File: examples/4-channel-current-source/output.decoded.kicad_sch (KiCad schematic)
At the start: 25 parts, among them IC12 ULQ2003AQDRQ1, Q4 BSS84Q-13-F, Q5 BSS84Q-13-F, Q6 BSS84Q-13-F, Q7 BSS84Q-13-F

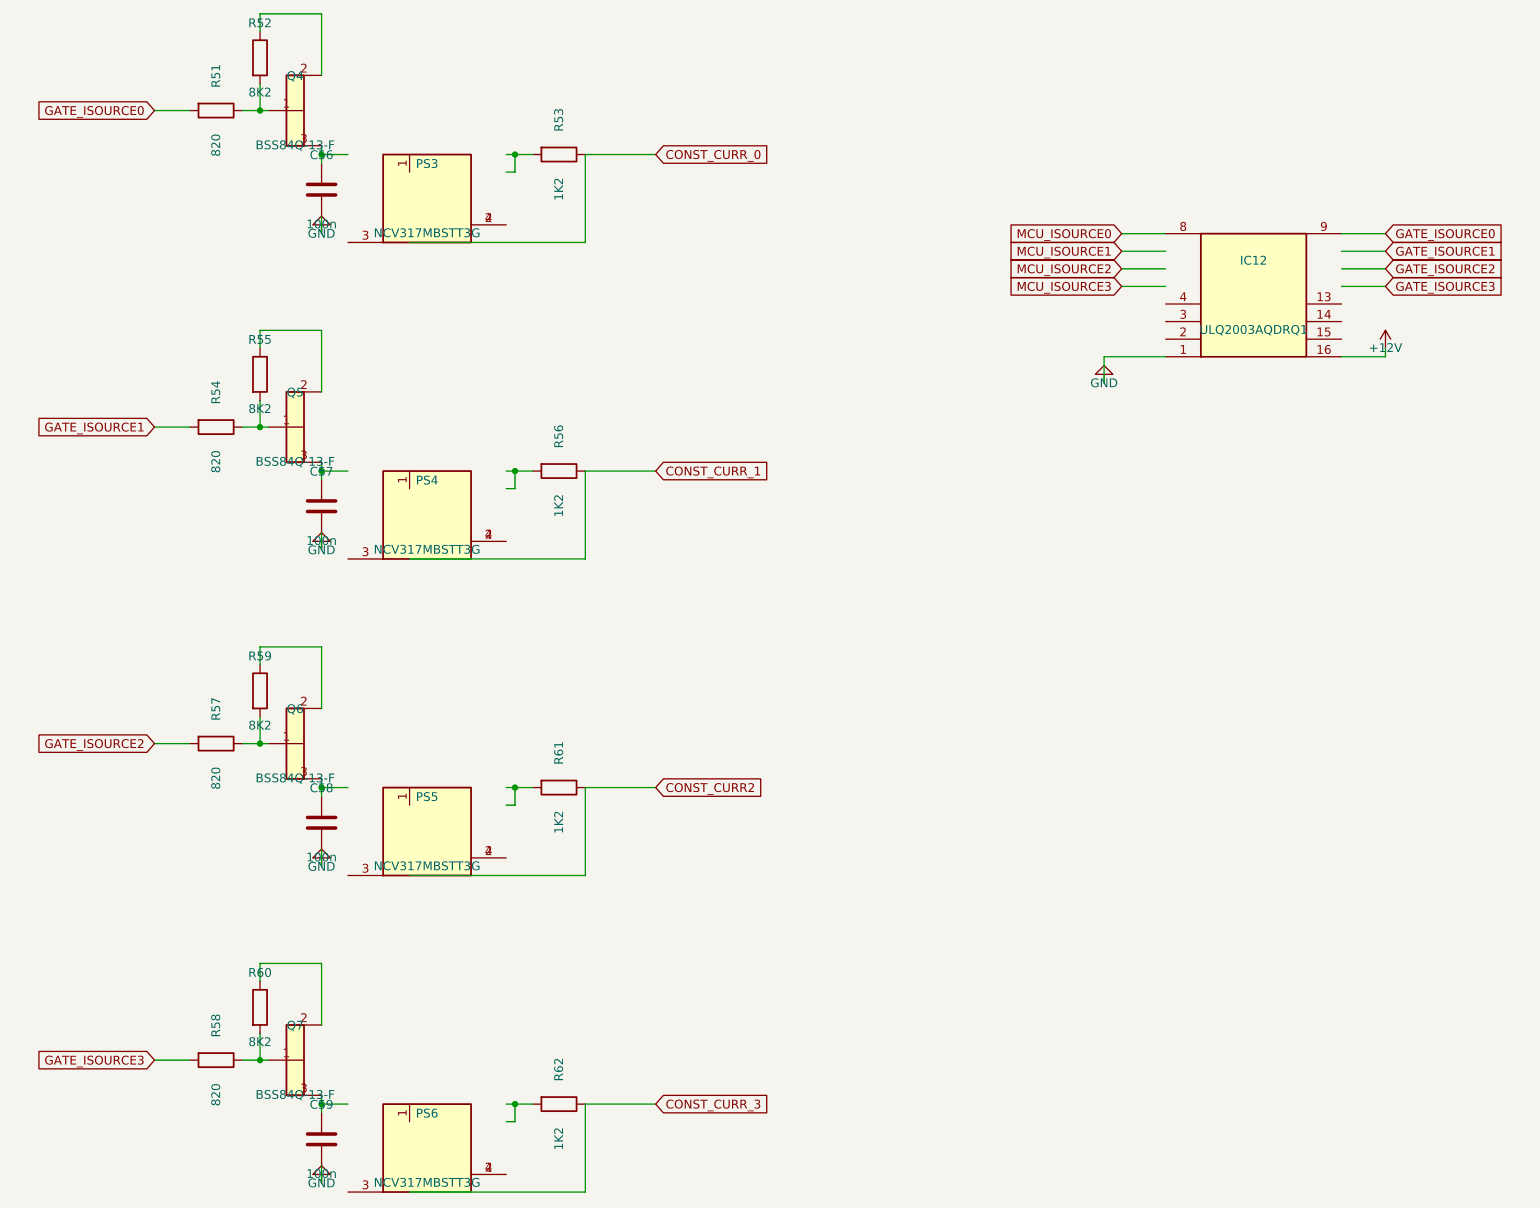
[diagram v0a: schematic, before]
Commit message: Add footprint lookup table for TOKN decoder
- Add footprints.json with comprehensive lookup table:
  - Common passive sizes (0402, 0603, 0805, etc.)
  - IC packages (SOIC, TSSOP, QFN, LQFP, etc.)
  - Specific parts (MCP2551, MAX232, ATmega, STM32, etc.)
  - Transistors, regulators, op-amps, and more

- Update tokn_decoder.py to auto-populate footprints:
  - Priority: explicit > package hint > part match > passive type
  - Handles size codes (0603) for passives automatically

Decoded schematics now have proper footprints ready for PCB layout.
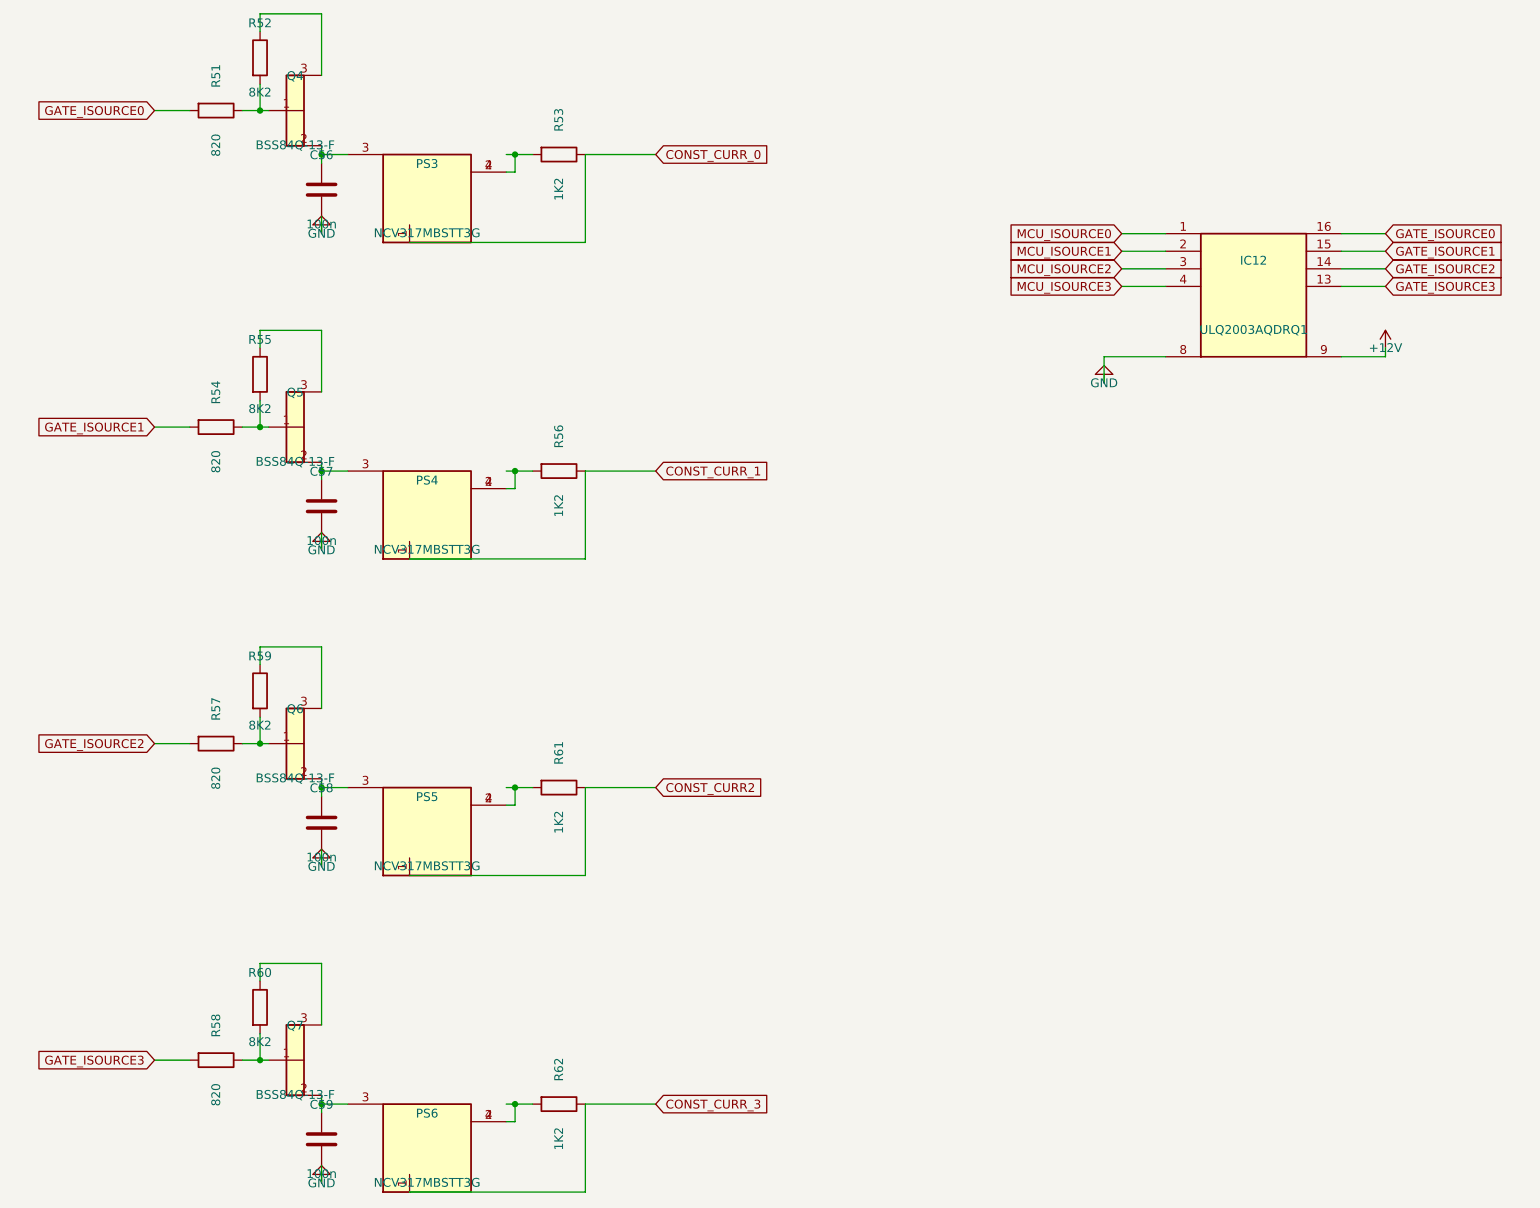
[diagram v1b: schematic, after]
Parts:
- C56, C57, C58, C59: footprint (none) -> Capacitor_SMD:C_0603_1608Metric
- IC12: footprint SOIC-127 -> Package_SO:SOIC-16_3.9x9.9mm_P1.27mm
- PS3, PS4, PS5, PS6: footprint SOT230P700X175-4N -> (none)
- Q4, Q5, Q6, Q7: footprint SOT-23 -> Package_TO_SOT_SMD:SOT-23
- R51, R52, R53, R54, R55, R56, R57, R58, R59, R60, R61, R62: footprint 0603 -> Resistor_SMD:R_0603_1608Metric
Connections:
- net +12V: now also IC12.9; no longer IC12.16
- net CONST_CURR2: now also PS5.1
- net CONST_CURR_0: now also PS3.1
- net CONST_CURR_1: now also PS4.1
- net CONST_CURR_3: now also PS6.1
- net GATE_ISOURCE0: now also IC12.16; no longer IC12.9
- net GATE_ISOURCE1: now also IC12.15
- net GATE_ISOURCE2: now also IC12.14
- net GATE_ISOURCE3: now also IC12.13
- net GND: now also IC12.8; no longer IC12.1
- net MCU_ISOURCE0: now also IC12.1; no longer IC12.8
- net MCU_ISOURCE1: now also IC12.2
- net MCU_ISOURCE2: now also IC12.3
- net MCU_ISOURCE3: now also IC12.4
- net at R60.1: now also Q7.3; no longer Q7.2
- net at PS5.2, PS5.4: now also R61.2
- net at PS5.3: now also C58.1, Q6.2
- net at R55.1: now also Q5.3; no longer Q5.2
- net at C56.1: now also PS3.3, Q4.2; no longer Q4.3
- net at R59.1: now also Q6.3; no longer Q6.2
- net at R56.2: now also PS4.2, PS4.4
- net at PS4.3: now also C57.1, Q5.2
- net at R53.2: now also PS3.2, PS3.4
- net at R52.1: now also Q4.3; no longer Q4.2
- net at C59.1: now also PS6.3, Q7.2; no longer Q7.3
- net at PS6.2, PS6.4: now also R62.2
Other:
- moved on the sheet: PS3, PS4, PS5, PS6
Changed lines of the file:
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@@
       (at 74.93 51.99 0)
       (effects (font (size 1.27 1.27))))
-    (property "Footprint" ""
+    (property "Footprint" "Capacitor_SMD:C_0603_1608Metric"
       (at 74.93 46.99 0)
       (effects (font (size 1.27 1.27)) (hide yes)))
@@
       (at 74.93 97.71 0)
       (effects (font (size 1.27 1.27))))
-    (property "Footprint" ""
+    (property "Footprint" "Capacitor_SMD:C_0603_1608Metric"
       (at 74.93 92.71 0)
       (effects (font (size 1.27 1.27)) (hide yes)))
@@
       (at 74.93 143.43 0)
       (effects (font (size 1.27 1.27))))
-    (property "Footprint" ""
+    (property "Footprint" "Capacitor_SMD:C_0603_1608Metric"
       (at 74.93 138.43 0)
       (effects (font (size 1.27 1.27)) (hide yes)))
@@
       (at 74.93 189.15 0)
       (effects (font (size 1.27 1.27))))
-    (property "Footprint" ""
+    (property "Footprint" "Capacitor_SMD:C_0603_1608Metric"
       (at 74.93 184.15 0)
       (effects (font (size 1.27 1.27)) (hide yes)))
@@
       (at 209.55 67.22999999999999 0)
       (effects (font (size 1.27 1.27))))
-    (property "Footprint" "SOIC-127"
+    (property "Footprint" "Package_SO:SOIC-16_3.9x9.9mm_P1.27mm"
       (at 209.55 62.23 0)
       (effects (font (size 1.27 1.27)) (hide yes)))
@@
       (at 90.17 53.26 0)
       (effects (font (size 1.27 1.27))))
-    (property "Footprint" "SOT230P700X175-4N"
+    (property "Footprint" ""
       (at 90.17 48.26 0)
       (effects (font (size 1.27 1.27)) (hide yes)))
@@
       (at 90.17 98.98 0)
       (effects (font (size 1.27 1.27))))
-    (property "Footprint" "SOT230P700X175-4N"
+    (property "Footprint" ""
       (at 90.17 93.98 0)
       (effects (font (size 1.27 1.27)) (hide yes)))
@@
       (at 90.17 144.7 0)
       (effects (font (size 1.27 1.27))))
-    (property "Footprint" "SOT230P700X175-4N"
+    (property "Footprint" ""
       (at 90.17 139.7 0)
       (effects (font (size 1.27 1.27)) (hide yes)))
@@
       (at 90.17 190.42 0)
       (effects (font (size 1.27 1.27))))
-    (property "Footprint" "SOT230P700X175-4N"
+    (property "Footprint" ""
       (at 90.17 185.42 0)
       (effects (font (size 1.27 1.27)) (hide yes)))
@@
       (at 71.12 40.56 0)
       (effects (font (size 1.27 1.27))))
-    (property "Footprint" "SOT-23"
+    (property "Footprint" "Package_TO_SOT_SMD:SOT-23"
       (at 71.12 35.56 0)
       (effects (font (size 1.27 1.27)) (hide yes)))
@@
       (at 71.12 86.28 0)
       (effects (font (size 1.27 1.27))))
-    (property "Footprint" "SOT-23"
+    (property "Footprint" "Package_TO_SOT_SMD:SOT-23"
       (at 71.12 81.28 0)
       (effects (font (size 1.27 1.27)) (hide yes)))
@@
       (at 71.12 132.0 0)
       (effects (font (size 1.27 1.27))))
-    (property "Footprint" "SOT-23"
+    (property "Footprint" "Package_TO_SOT_SMD:SOT-23"
       (at 71.12 127.0 0)
       (effects (font (size 1.27 1.27)) (hide yes)))
@@
       (at 71.12 177.72 0)
       (effects (font (size 1.27 1.27))))
-    (property "Footprint" "SOT-23"
+    (property "Footprint" "Package_TO_SOT_SMD:SOT-23"
       (at 71.12 172.72 0)
       (effects (font (size 1.27 1.27)) (hide yes)))
@@
       (at 59.69 40.56 0)
       (effects (font (size 1.27 1.27))))
-    (property "Footprint" "0603"
+    (property "Footprint" "Resistor_SMD:R_0603_1608Metric"
       (at 59.69 35.56 0)
       (effects (font (size 1.27 1.27)) (hide yes)))
@@
       (at 66.04 32.94 0)
       (effects (font (size 1.27 1.27))))
-    (property "Footprint" "0603"
+    (property "Footprint" "Resistor_SMD:R_0603_1608Metric"
       (at 66.04 27.94 0)
       (effects (font (size 1.27 1.27)) (hide yes)))
@@
       (at 109.22 46.91 0)
       (effects (font (size 1.27 1.27))))
-    (property "Footprint" "0603"
+    (property "Footprint" "Resistor_SMD:R_0603_1608Metric"
       (at 109.22 41.91 0)
       (effects (font (size 1.27 1.27)) (hide yes)))
@@
       (at 59.69 86.28 0)
       (effects (font (size 1.27 1.27))))
-    (property "Footprint" "0603"
+    (property "Footprint" "Resistor_SMD:R_0603_1608Metric"
       (at 59.69 81.28 0)
       (effects (font (size 1.27 1.27)) (hide yes)))
@@
       (at 66.04 78.66 0)
       (effects (font (size 1.27 1.27))))
-    (property "Footprint" "0603"
+    (property "Footprint" "Resistor_SMD:R_0603_1608Metric"
       (at 66.04 73.66 0)
       (effects (font (size 1.27 1.27)) (hide yes)))
@@
       (at 109.22 92.63 0)
       (effects (font (size 1.27 1.27))))
-    (property "Footprint" "0603"
+    (property "Footprint" "Resistor_SMD:R_0603_1608Metric"
       (at 109.22 87.63 0)
       (effects (font (size 1.27 1.27)) (hide yes)))
@@
       (at 59.69 132.0 0)
       (effects (font (size 1.27 1.27))))
-    (property "Footprint" "0603"
+    (property "Footprint" "Resistor_SMD:R_0603_1608Metric"
       (at 59.69 127.0 0)
       (effects (font (size 1.27 1.27)) (hide yes)))
@@
       (at 59.69 177.72 0)
       (effects (font (size 1.27 1.27))))
-    (property "Footprint" "0603"
+    (property "Footprint" "Resistor_SMD:R_0603_1608Metric"
       (at 59.69 172.72 0)
       (effects (font (size 1.27 1.27)) (hide yes)))
@@
       (at 66.04 124.38 0)
       (effects (font (size 1.27 1.27))))
-    (property "Footprint" "0603"
+    (property "Footprint" "Resistor_SMD:R_0603_1608Metric"
       (at 66.04 119.38 0)
       (effects (font (size 1.27 1.27)) (hide yes)))
@@
       (at 66.04 170.1 0)
       (effects (font (size 1.27 1.27))))
-    (property "Footprint" "0603"
+    (property "Footprint" "Resistor_SMD:R_0603_1608Metric"
       (at 66.04 165.1 0)
       (effects (font (size 1.27 1.27)) (hide yes)))
@@
       (at 109.22 138.35 0)
       (effects (font (size 1.27 1.27))))
-    (property "Footprint" "0603"
+    (property "Footprint" "Resistor_SMD:R_0603_1608Metric"
       (at 109.22 133.35 0)
       (effects (font (size 1.27 1.27)) (hide yes)))
@@
       (at 109.22 184.07 0)
       (effects (font (size 1.27 1.27))))
-    (property "Footprint" "0603"
+    (property "Footprint" "Resistor_SMD:R_0603_1608Metric"
       (at 109.22 179.07 0)
       (effects (font (size 1.27 1.27)) (hide yes)))

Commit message: Fix decoder pin placement using TOKN pins section
- Use pin definitions from TOKN pins{REF}[N]: section instead of
  deriving positions from wire endpoints
- Calculate pin positions using standard dual-inline IC layout:
  pins 1-N/2 on left (top to bottom), N/2+1 to N on right (bottom to top)
- Include pin names from TOKN in generated lib_symbols
- Fix issue where pins with same net were merged to same position
- Regenerate all decoded schematics with correct pin placement
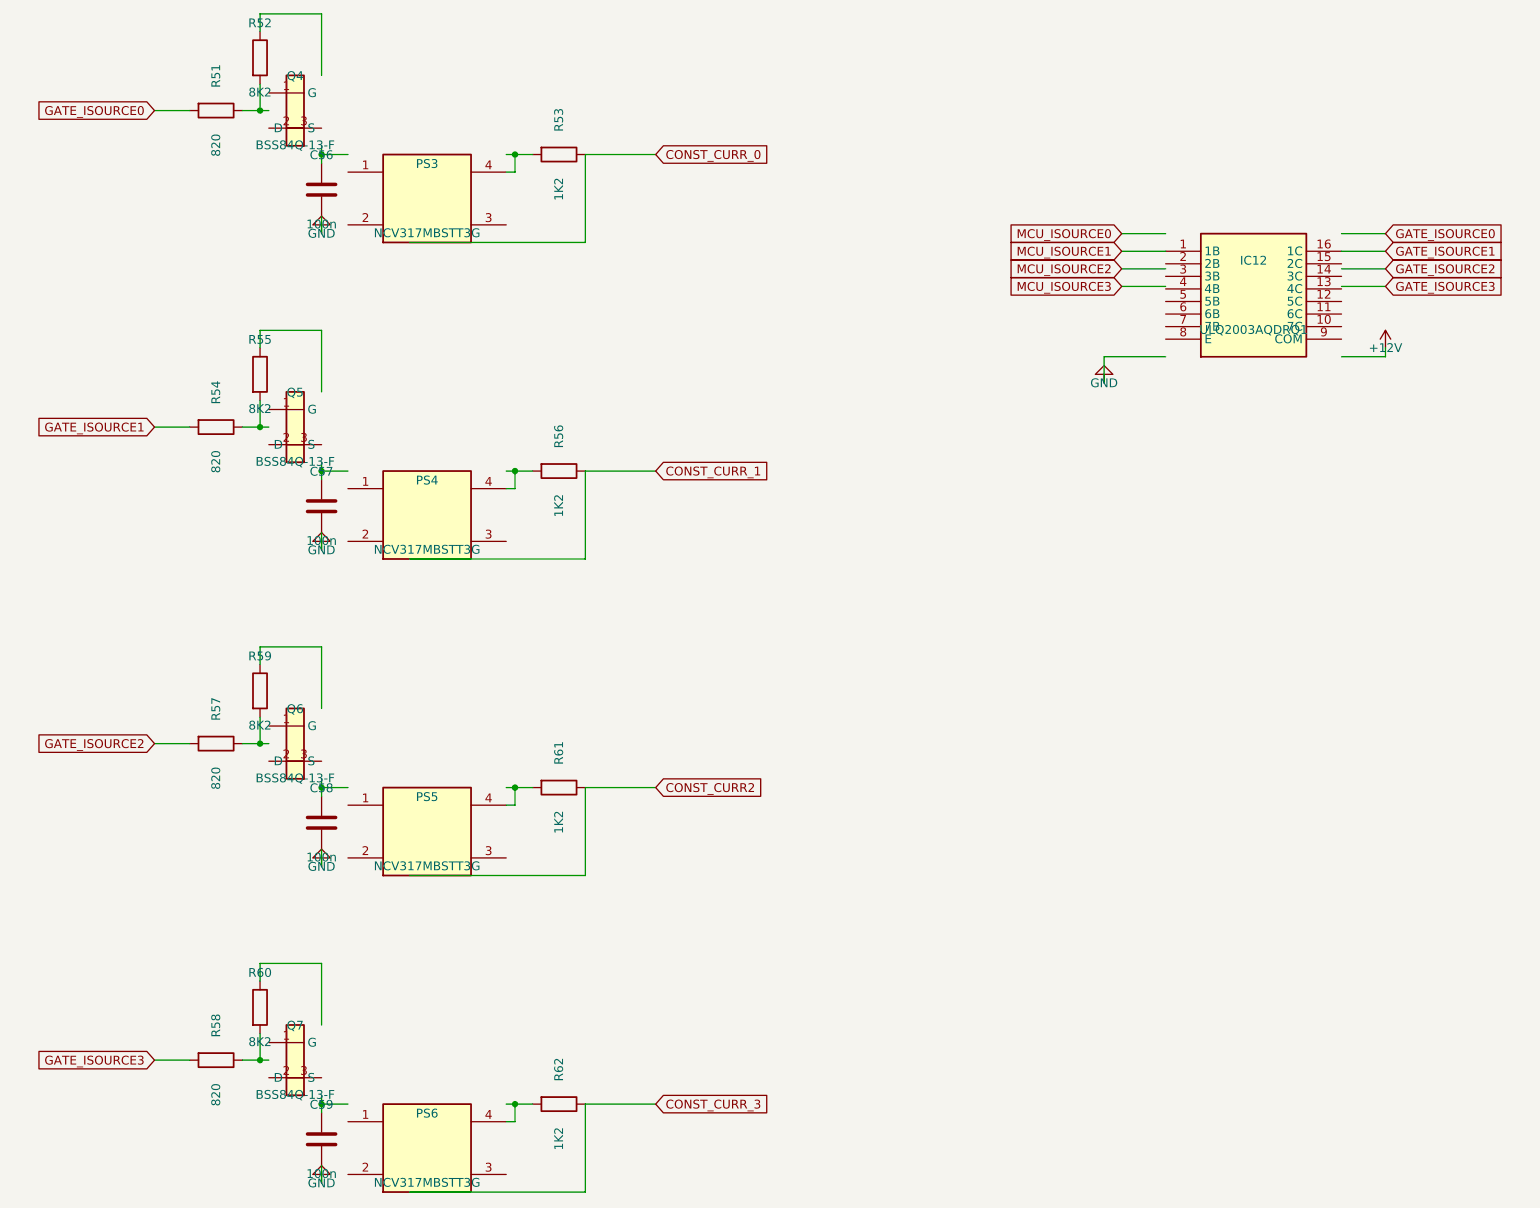
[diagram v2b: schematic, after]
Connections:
- net +12V: no longer IC12.9
- net CONST_CURR2: no longer PS5.1
- net CONST_CURR_0: no longer PS3.1
- net CONST_CURR_1: no longer PS4.1
- net CONST_CURR_3: no longer PS6.1
- net GATE_ISOURCE0: no longer IC12.16
- net GATE_ISOURCE1: now also IC12.16 (1C); no longer IC12.15
- net GATE_ISOURCE2: no longer IC12.14
- net GATE_ISOURCE3: no longer IC12.13
- net GND: no longer IC12.8
- net MCU_ISOURCE0: no longer IC12.1
- net MCU_ISOURCE1: now also IC12.1 (1B); no longer IC12.2
- net MCU_ISOURCE2: no longer IC12.3
- net MCU_ISOURCE3: no longer IC12.4
- net at R60.1: no longer Q7.3
- net at R58.1, R60.2: no longer Q7.1
- net at PS5.4, R61.2: no longer PS5.2
- net at R55.1: no longer Q5.3
- net at R54.1, R55.2: no longer Q5.1
- net at R57.1, R59.2: no longer Q6.1
- net at Q6.3 (D): no longer R59.1
- net at PS4.4, R56.2: no longer PS4.2
- net at PS3.4, R53.2: no longer PS3.2
- net at R51.1, R52.2: no longer Q4.1
- net at R52.1: no longer Q4.3
- net at PS6.4, R62.2: no longer PS6.2
- now unconnected: C56.1, C57.1, C58.1, C59.1, PS3.3, PS4.3, PS5.3, PS6.3, Q4.2, Q5.2, Q6.2, Q7.2
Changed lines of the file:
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@@
       (at 209.55 62.23 0)
       (effects (font (size 1.27 1.27)) (hide yes)))
+    (pin "1"
+    )
+    (pin "2"
+    )
+    (pin "3"
+    )
+    (pin "4"
+    )
+    (pin "5"
+    )
+    (pin "6"
+    )
+    (pin "7"
+    )
+    (pin "8"
+    )
     (pin "9"
     )
-    (pin "8"
+    (pin "10"
+    )
+    (pin "11"
+    )
+    (pin "12"
+    )
+    (pin "13"
+    )
+    (pin "14"
+    )
+    (pin "15"
     )
     (pin "16"
-    )
-    (pin "15"
-    )
-    (pin "14"
-    )
-    (pin "13"
-    )
-    (pin "1"
-    )
-    (pin "2"
-    )
-    (pin "3"
-    )
-    (pin "4"
     )
     (instances
@@
       (at 71.12 35.56 0)
       (effects (font (size 1.27 1.27)) (hide yes)))
-    (pin "3"
-    )
-    (pin "1"
-    )
-    (pin "2"
+    (pin "1"
+    )
+    (pin "2"
+    )
+    (pin "3"
     )
     (instances
@@
       (at 71.12 81.28 0)
       (effects (font (size 1.27 1.27)) (hide yes)))
-    (pin "3"
-    )
-    (pin "2"
-    )
-    (pin "1"
+    (pin "1"
+    )
+    (pin "2"
+    )
+    (pin "3"
     )
     (instances
@@
       (at 71.12 127.0 0)
       (effects (font (size 1.27 1.27)) (hide yes)))
-    (pin "3"
-    )
-    (pin "2"
-    )
-    (pin "1"
+    (pin "1"
+    )
+    (pin "2"
+    )
+    (pin "3"
     )
     (instances
@@
       (at 71.12 172.72 0)
       (effects (font (size 1.27 1.27)) (hide yes)))
-    (pin "3"
-    )
-    (pin "1"
-    )
-    (pin "2"
-    )
-    (instances
+    (pin "1"
+    )
+    (pin "2"
+    )
+    (pin "3"
+    )
+    (instances
